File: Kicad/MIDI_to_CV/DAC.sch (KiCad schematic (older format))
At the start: 13 parts, among them U2 MCP4921, U3 MCP4921, U4 LM358, U5 MCP4921, U6 LM358

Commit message: Adding lots of decoupling capacitors
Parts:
- added C10, C11, C12, C13, C9: 0.01uF, symbol Device:C
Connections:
- net 12V: now also C12.1, C13.1
- net 3.3V: now also C10.1, C11.1, C9.1
- net GND: now also C10.2, C11.2, C12.2, C13.2, C9.2
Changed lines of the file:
@@
 Text HLabel 5100 2100 0    50   Input ~ 0
 12V
+$Comp
+L Device:C C9
+U 1 1 5FC72602
+P 2200 1000
+F 0 "C9" V 1948 1000 50  0000 C CNN
+F 1 "0.01uF" V 2039 1000 50  0000 C CNN
+F 2 "" H 2238 850 50  0001 C CNN
+F 3 "~" H 2200 1000 50  0001 C CNN
+	1    2200 1000
+	0    1    1    0
+$EndComp
+$Comp
+L Device:C C10
+U 1 1 5FC73AFB
+P 2250 2500
+F 0 "C10" V 1998 2500 50  0000 C CNN
+F 1 "0.01uF" V 2089 2500 50  0000 C CNN
+F 2 "" H 2288 2350 50  0001 C CNN
+F 3 "~" H 2250 2500 50  0001 C CNN
+	1    2250 2500
+	0    1    1    0
+$EndComp
+$Comp
+L Device:C C11
+U 1 1 5FC74208
+P 2250 3950
+F 0 "C11" V 1998 3950 50  0000 C CNN
+F 1 "0.01uF" V 2089 3950 50  0000 C CNN
+F 2 "" H 2288 3800 50  0001 C CNN
+F 3 "~" H 2250 3950 50  0001 C CNN
+	1    2250 3950
+	0    1    1    0
+$EndComp
+Text HLabel 2100 3950 0    50   Input ~ 0
+GND
+Text HLabel 2100 2500 0    50   Input ~ 0
+GND
+Text HLabel 2050 1000 0    50   Input ~ 0
+GND
+$Comp
+L Device:C C12
+U 1 1 5FC754B0
+P 4900 2450
+F 0 "C12" H 5015 2496 50  0000 L CNN
+F 1 "0.01uF" H 5015 2405 50  0000 L CNN
+F 2 "" H 4938 2300 50  0001 C CNN
+F 3 "~" H 4900 2450 50  0001 C CNN
+	1    4900 2450
+	1    0    0    -1
+$EndComp
+Wire Wire Line
+	5100 2250 4900 2250
+Wire Wire Line
+	4900 2250 4900 2300
+Wire Wire Line
+	5100 2600 4900 2600
+$Comp
+L Device:C C13
+U 1 1 5FC796CE
+P 4900 5650
+F 0 "C13" H 5015 5696 50  0000 L CNN
+F 1 "0.01uF" H 5015 5605 50  0000 L CNN
+F 2 "" H 4938 5500 50  0001 C CNN
+F 3 "~" H 4900 5650 50  0001 C CNN
+	1    4900 5650
+	1    0    0    -1
+$EndComp
+Wire Wire Line
+	5200 5800 4900 5800
+Wire Wire Line
+	5200 5500 4900 5500
+Wire Wire Line
+	5200 5350 5200 5500
+Connection ~ 5200 5350
+Wire Wire Line
+	5200 5800 5200 5950
+Wire Wire Line
+	5100 2250 5100 2100
+Connection ~ 5100 2100
+Wire Wire Line
+	5100 2600 5100 2700
 $EndSCHEMATC

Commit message: Added output resistors
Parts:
- added R13, R14, R15, R16: 1K, symbol Device:R
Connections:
- net CV1: now also R13.1; no longer R5.1, U4.1
- net CV2: now also R14.1; no longer R6.1, U4.7
- net CV3: now also R15.1; no longer R9.1, U6.1
- net GATE: now also R16.1; no longer R10.1, U6.7
- new net: R13.2, R5.1, U4.1
- new net: R14.2, R6.1, U4.7
- new net: R15.2, R9.1, U6.1
- new net: R10.1, R16.2, U6.7
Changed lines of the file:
@@
 Wire Wire Line
 	4250 6350 3600 6350
-Text HLabel 5450 6450 2    50   Output ~ 0
+Text HLabel 5150 6450 2    50   Output ~ 0
 GATE
 Text HLabel 5150 4450 2    50   Output ~ 0
@@
 CV1
 Wire Wire Line
-	4800 1500 5150 1500
+	4800 1500 4850 1500
 Connection ~ 4800 1500
-Wire Wire Line
-	4850 3000 5150 3000
-Connection ~ 4850 3000
-Wire Wire Line
-	4850 4450 5150 4450
-Connection ~ 4850 4450
-Wire Wire Line
-	4850 6450 5450 6450
-Connection ~ 4850 6450
 Wire Wire Line
 	2350 1800 3850 1800
@@
 Wire Wire Line
 	5100 2600 5100 2700
+$Comp
+L Device:R R13
+U 1 1 5FCB2CC0
+P 5000 1500
+F 0 "R13" V 4793 1500 50  0000 C CNN
+F 1 "1K" V 4884 1500 50  0000 C CNN
+F 2 "" V 4930 1500 50  0001 C CNN
+F 3 "~" H 5000 1500 50  0001 C CNN
+	1    5000 1500
+	0    1    1    0
+$EndComp
+$Comp
+L Device:R R14
+U 1 1 5FCB4627
+P 5000 3000
+F 0 "R14" V 4793 3000 50  0000 C CNN
+F 1 "1K" V 4884 3000 50  0000 C CNN
+F 2 "" V 4930 3000 50  0001 C CNN
+F 3 "~" H 5000 3000 50  0001 C CNN
+	1    5000 3000
+	0    1    1    0
+$EndComp
+Connection ~ 4850 3000
+$Comp
+L Device:R R15
+U 1 1 5FCB4C4C
+P 5000 4450
+F 0 "R15" V 4793 4450 50  0000 C CNN
+F 1 "1K" V 4884 4450 50  0000 C CNN
+F 2 "" V 4930 4450 50  0001 C CNN
+F 3 "~" H 5000 4450 50  0001 C CNN
+	1    5000 4450
+	0    1    1    0
+$EndComp
+Connection ~ 4850 4450
+$Comp
+L Device:R R16
+U 1 1 5FCB6C40
+P 5000 6450
+F 0 "R16" V 4793 6450 50  0000 C CNN
+F 1 "1K" V 4884 6450 50  0000 C CNN
+F 2 "" V 4930 6450 50  0001 C CNN
+F 3 "~" H 5000 6450 50  0001 C CNN
+	1    5000 6450
+	0    1    1    0
+$EndComp
+Connection ~ 4850 6450
 $EndSCHEMATC

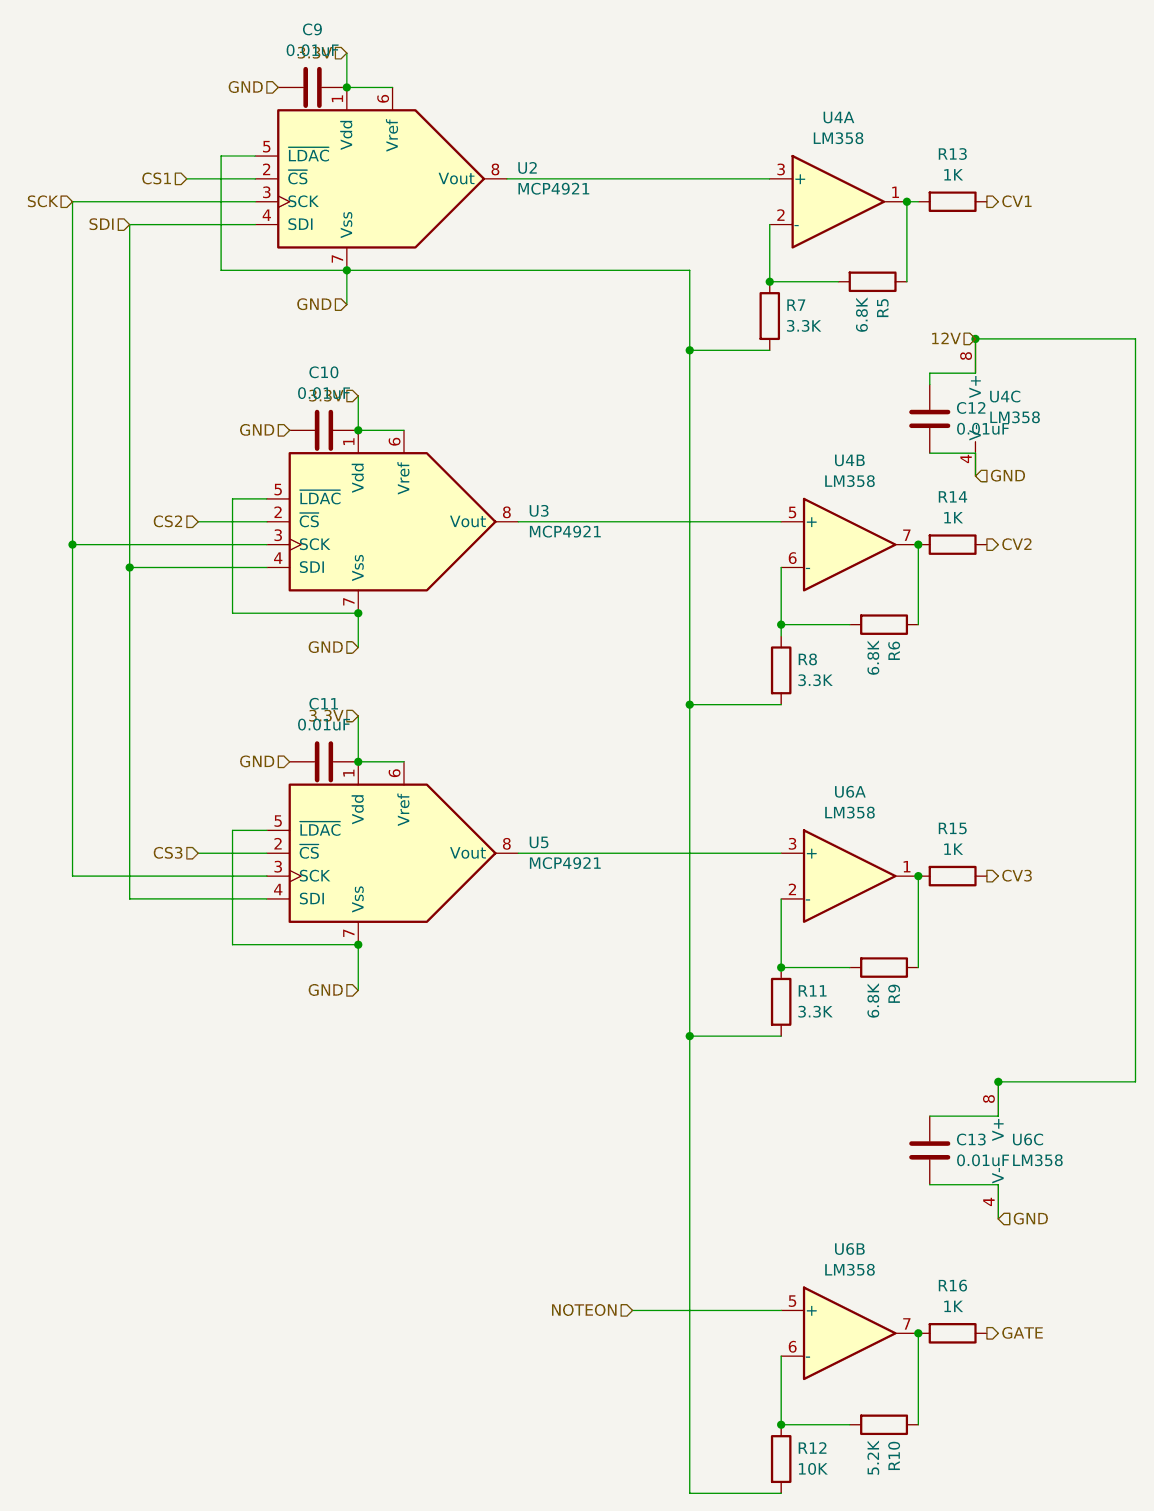
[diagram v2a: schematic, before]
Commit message: Changed size of decoupling capacitors
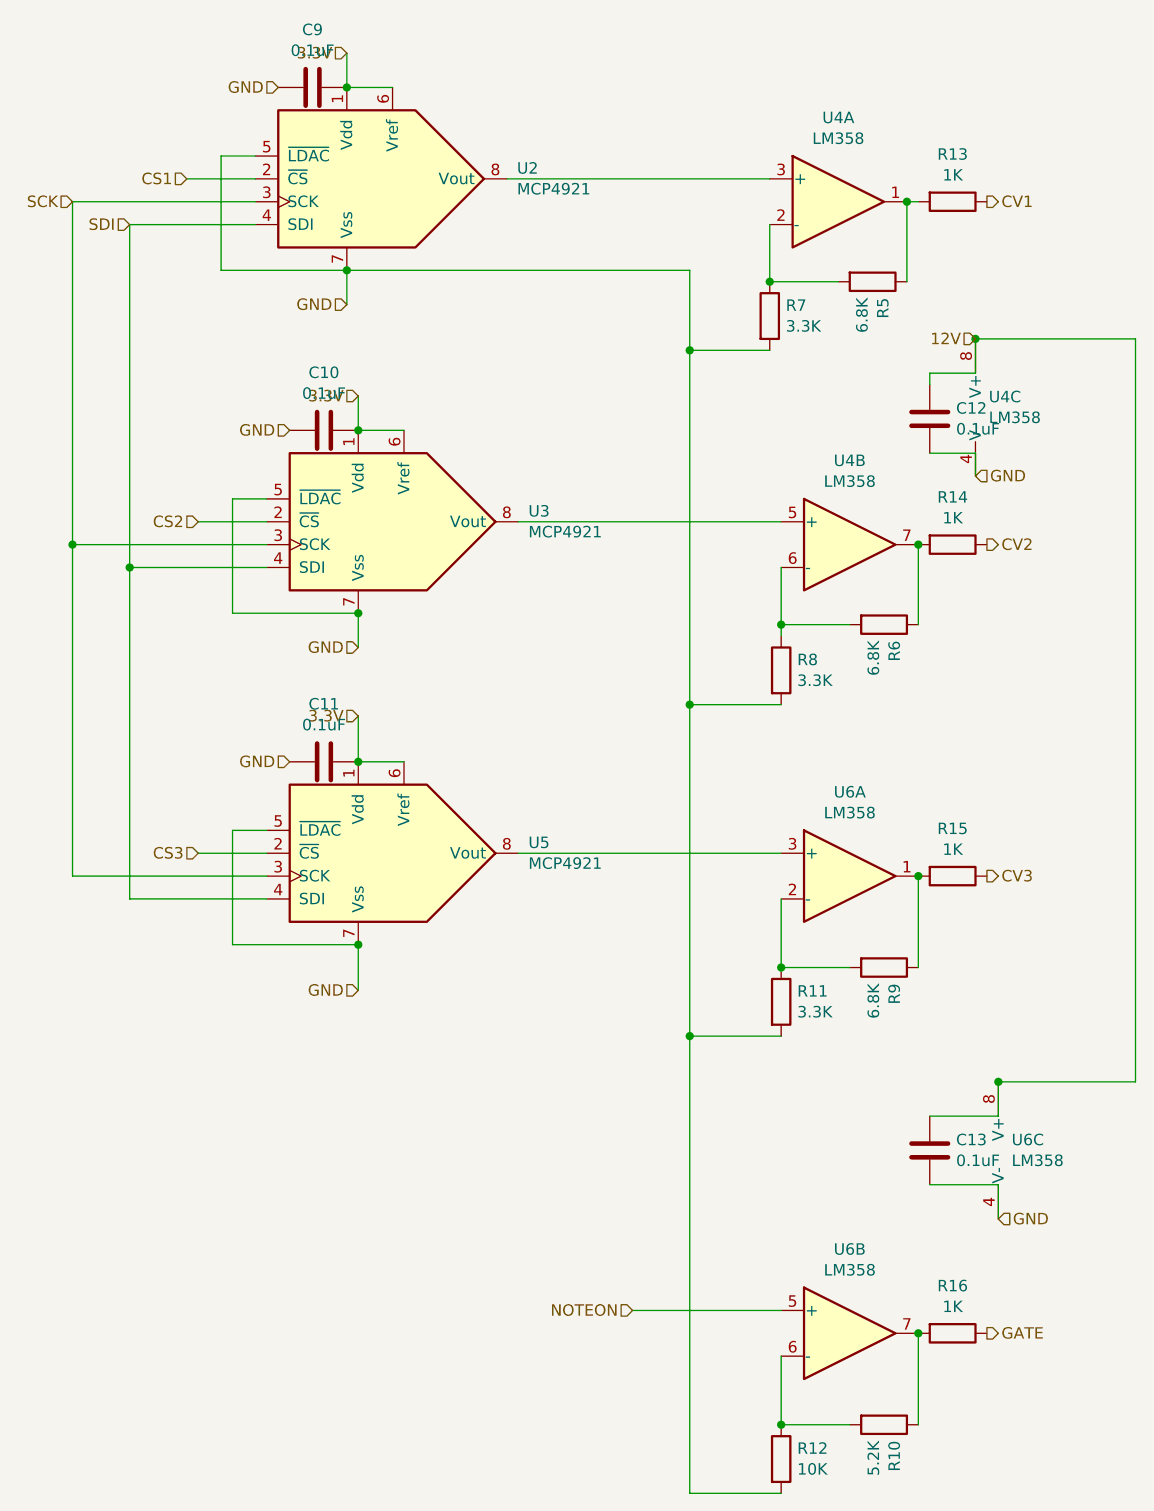
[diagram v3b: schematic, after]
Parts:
- C10, C11, C12, C13, C9: value 0.01uF -> 0.1uF
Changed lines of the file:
@@
 P 2200 1000
 F 0 "C9" V 1948 1000 50  0000 C CNN
-F 1 "0.01uF" V 2039 1000 50  0000 C CNN
+F 1 "0.1uF" V 2039 1000 50  0000 C CNN
 F 2 "" H 2238 850 50  0001 C CNN
 F 3 "~" H 2200 1000 50  0001 C CNN
@@
 P 2250 2500
 F 0 "C10" V 1998 2500 50  0000 C CNN
-F 1 "0.01uF" V 2089 2500 50  0000 C CNN
+F 1 "0.1uF" V 2089 2500 50  0000 C CNN
 F 2 "" H 2288 2350 50  0001 C CNN
 F 3 "~" H 2250 2500 50  0001 C CNN
@@
 P 2250 3950
 F 0 "C11" V 1998 3950 50  0000 C CNN
-F 1 "0.01uF" V 2089 3950 50  0000 C CNN
+F 1 "0.1uF" V 2089 3950 50  0000 C CNN
 F 2 "" H 2288 3800 50  0001 C CNN
 F 3 "~" H 2250 3950 50  0001 C CNN
@@
 P 4900 2450
 F 0 "C12" H 5015 2496 50  0000 L CNN
-F 1 "0.01uF" H 5015 2405 50  0000 L CNN
+F 1 "0.1uF" H 5015 2405 50  0000 L CNN
 F 2 "" H 4938 2300 50  0001 C CNN
 F 3 "~" H 4900 2450 50  0001 C CNN
@@
 P 4900 5650
 F 0 "C13" H 5015 5696 50  0000 L CNN
-F 1 "0.01uF" H 5015 5605 50  0000 L CNN
+F 1 "0.1uF" H 5015 5605 50  0000 L CNN
 F 2 "" H 4938 5500 50  0001 C CNN
 F 3 "~" H 4900 5650 50  0001 C CNN
